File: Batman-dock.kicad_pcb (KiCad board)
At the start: 2 copper layers, 42 x 12 mm, 5 parts, among them J1 TYPECL324LBCP24, J2 70AAJL6LM0G, J3 70AAJL6LM0G

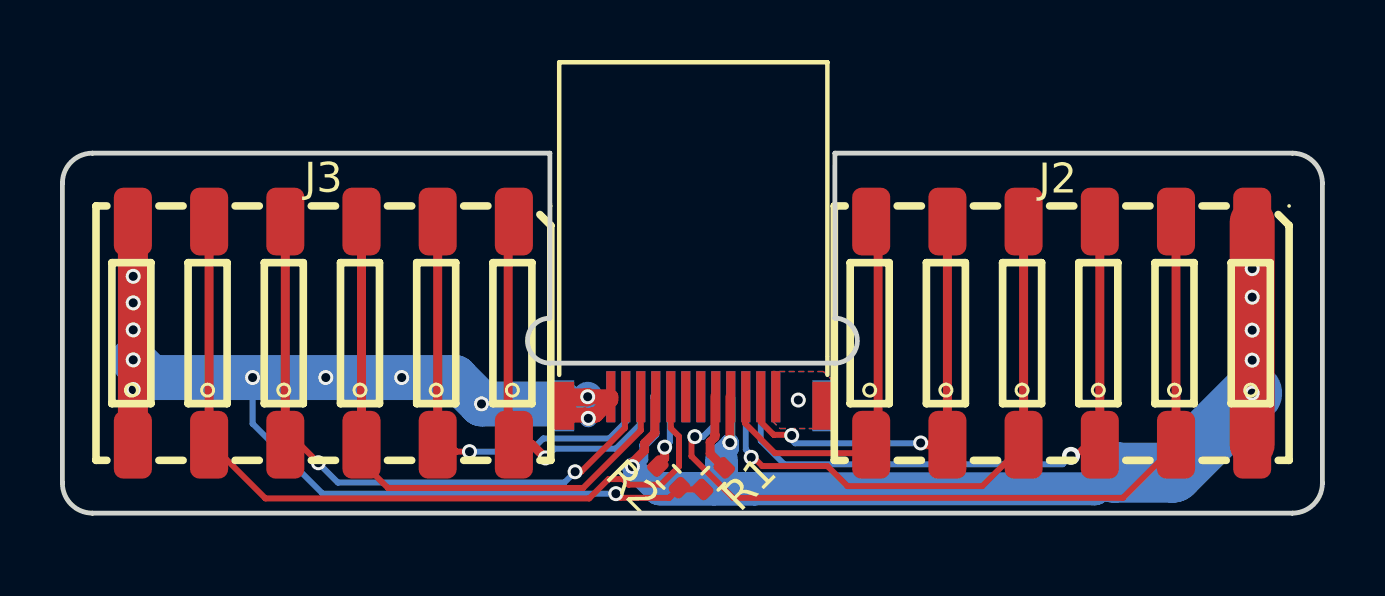
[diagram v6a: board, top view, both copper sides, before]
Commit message: Shorter PCB:  42mm -> 40mm
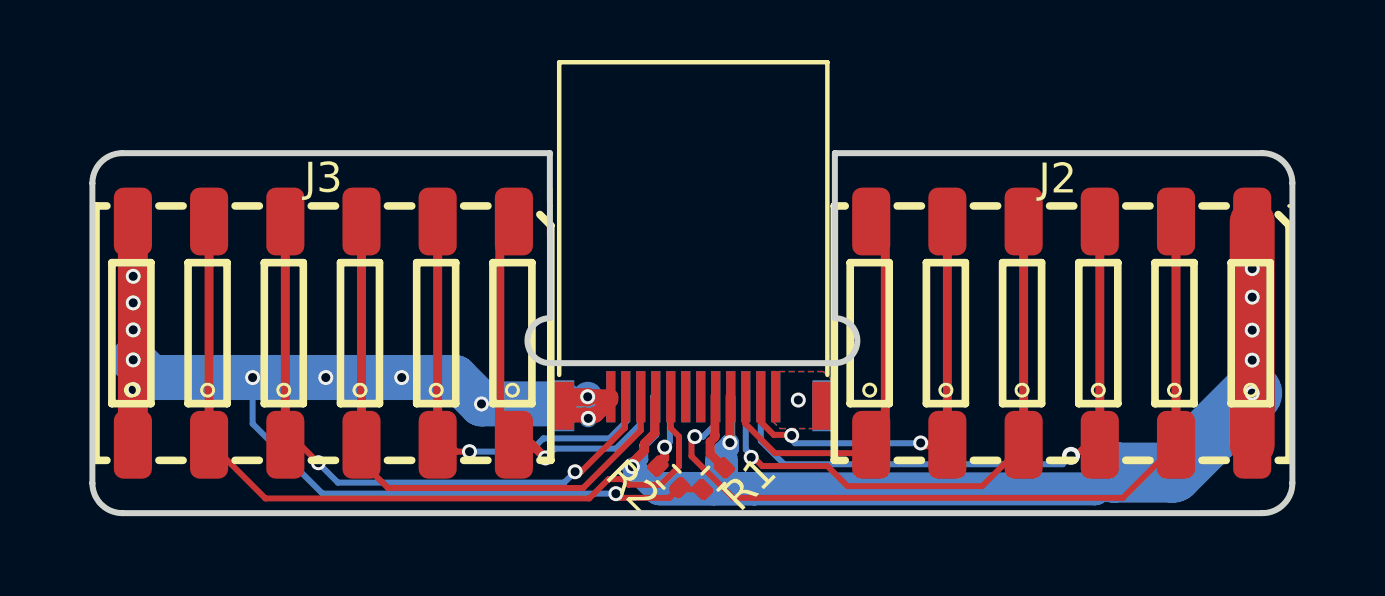
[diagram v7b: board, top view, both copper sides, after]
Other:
- board size 42 x 12 mm -> 40 x 12 mm
